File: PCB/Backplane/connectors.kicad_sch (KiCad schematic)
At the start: 10 parts, among them J2 Front, J3 Rear, J4 Bus In, J5 Bus Out, J6 Power In, J7 Power Out, U10 CM1293A‐04SO, U9 CM1293A‐04SO

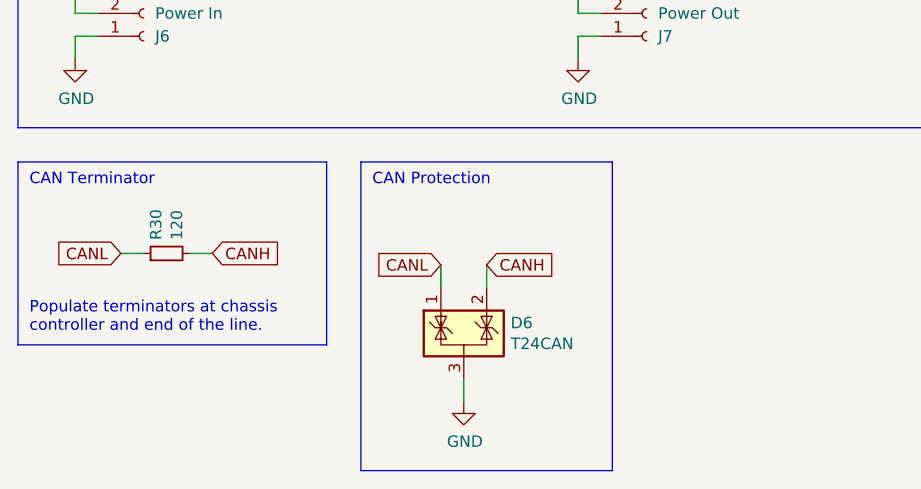
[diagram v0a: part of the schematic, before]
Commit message: Add ESD protection to the RS485 networks.
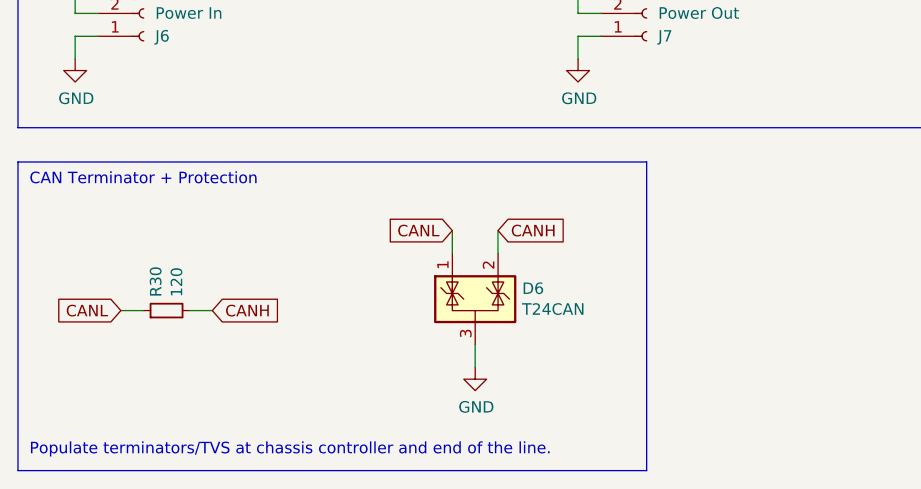
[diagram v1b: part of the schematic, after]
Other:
- note added: "CAN Terminator + Protection"
- note added: "Populate terminators/TVS at chassis controller and end of the line."
- note removed: "CAN Protection"
- note removed: "CAN Terminator"
- note removed: "Populate terminators at chassis controller and end of the line."
- moved on the sheet: D6, R30
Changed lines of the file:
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@@
 	(rectangle
 		(start 15.24 132.08)
-		(end 49.53 152.4)
+		(end 85.09 166.37)
 		(stroke
 			(width 0)
@@
 	)
 	(rectangle
-		(start 53.34 132.08)
-		(end 81.28 166.37)
-		(stroke
-			(width 0)
-			(type default)
-		)
-		(fill
-			(type none)
-		)
-	)
-	(rectangle
 		(start 165.1 15.24)
 		(end 275.59 71.12)
@@
 		)
 	)
-	(text "CAN Terminator"
+	(text "CAN Terminator + Protection"
 		(exclude_from_sim no)
 		(at 16.51 133.35 0)
@@
 		)
 	)
-	(text "Populate terminators at chassis\ncontroller and end of the line."
+	(text "Populate terminators/TVS at chassis controller and end of the line."
 		(exclude_from_sim no)
-		(at 16.51 151.13 0)
+		(at 16.51 164.846 0)
 		(effects
 			(font
@@
 		(exclude_from_sim no)
 		(at 166.37 16.51 0)
-		(effects
-			(font
-				(size 1.27 1.27)
-			)
-			(justify left top)
-		)
-	)
-	(text "CAN Protection"
-		(exclude_from_sim no)
-		(at 54.61 133.35 0)
 		(effects
 			(font
@@
 	(wire
 		(pts
-			(xy 64.77 156.21) (xy 64.77 158.75)
+			(xy 66.04 152.4) (xy 66.04 154.94)
 		)
 		(stroke
@@
 	(wire
 		(pts
-			(xy 26.67 142.24) (xy 29.21 142.24)
+			(xy 26.67 148.59) (xy 29.21 148.59)
 		)
 		(stroke
@@
 	(wire
 		(pts
-			(xy 67.31 143.51) (xy 67.31 146.05)
+			(xy 68.58 139.7) (xy 68.58 142.24)
 		)
 		(stroke
@@
 	(wire
 		(pts
-			(xy 62.23 143.51) (xy 62.23 146.05)
+			(xy 63.5 139.7) (xy 63.5 142.24)
 		)
 		(stroke
@@
 	(wire
 		(pts
-			(xy 36.83 142.24) (xy 34.29 142.24)
+			(xy 36.83 148.59) (xy 34.29 148.59)
 		)
 		(stroke
@@
 	(global_label "CANH"
 		(shape input)
-		(at 36.83 142.24 0)
+		(at 36.83 148.59 0)
 		(fields_autoplaced yes)
 		(effects
@@
 		)
 		(property "Intersheetrefs" "${INTERSHEET_REFS}"
-			(at 44.8348 142.24 0)
+			(at 44.8348 148.59 0)
 			(effects
 				(font
@@
 	(global_label "CANL"
 		(shape input)
-		(at 26.67 142.24 180)
+		(at 26.67 148.59 180)
 		(fields_autoplaced yes)
 		(effects
@@
 		)
 		(property "Intersheetrefs" "${INTERSHEET_REFS}"
-			(at 19.6218 142.24 0)
+			(at 19.6218 148.59 0)
 			(effects
 				(font
@@
 	(global_label "CANL"
 		(shape input)
-		(at 62.23 143.51 180)
+		(at 63.5 139.7 180)
 		(fields_autoplaced yes)
 		(effects
@@
 		)
 		(property "Intersheetrefs" "${INTERSHEET_REFS}"
-			(at 55.1818 143.51 0)
+			(at 56.4518 139.7 0)
 			(effects
 				(font
@@
 	(global_label "CANH"
 		(shape input)
-		(at 67.31 143.51 0)
+		(at 68.58 139.7 0)
 		(fields_autoplaced yes)
 		(effects
@@
 		)
 		(property "Intersheetrefs" "${INTERSHEET_REFS}"
-			(at 74.6606 143.51 0)
+			(at 75.9306 139.7 0)
 			(effects
 				(font
@@
 	(symbol
 		(lib_id "Power_Protection:NUP2105L")
-		(at 64.77 151.13 0)
+		(at 66.04 147.32 0)
 		(unit 1)
 		(exclude_from_sim no)
@@
 		(dnp no)
 		(property "Reference" "D6"
-			(at 69.977 149.9616 0)
+			(at 71.247 146.1516 0)
 			(effects
 				(font
@@
 		)
 		(property "Value" "T24CAN"
-			(at 69.977 152.273 0)
+			(at 71.247 148.463 0)
 			(effects
 				(font
@@
 		)
 		(property "Footprint" "Package_TO_SOT_SMD:SOT-23"
-			(at 70.485 152.4 0)
+			(at 71.755 148.59 0)
 			(effects
 				(font
@@
 		)
 		(property "Datasheet" "https://www.onsemi.com/pub_link/Collateral/NUP2105L-D.PDF"
-			(at 67.945 147.955 0)
+			(at 69.215 144.145 0)
 			(effects
 				(font
@@
 		)
 		(property "Description" "Dual Line CAN Bus Protector, 24Vrwm"
-			(at 64.77 151.13 0)
+			(at 66.04 147.32 0)
 			(effects
 				(font
@@
 		)
 		(property "DIGIKEY" "STOCK"
-			(at 64.77 151.13 0)
+			(at 66.04 147.32 0)
 			(effects
 				(font
@@
 		)
 		(property "Sim.Device" ""
-			(at 64.77 151.13 0)
+			(at 66.04 147.32 0)
 			(effects
 				(font
@@
 		)
 		(property "Sim.Pins" ""
-			(at 64.77 151.13 0)
+			(at 66.04 147.32 0)
 			(effects
 				(font
@@
 	(symbol
 		(lib_id "power:GND")
-		(at 64.77 158.75 0)
+		(at 66.04 154.94 0)
 		(unit 1)
 		(exclude_from_sim no)
@@
 		(dnp no)
 		(property "Reference" "#PWR086"
-			(at 64.77 165.1 0)
+			(at 66.04 161.29 0)
 			(effects
 				(font
@@
 		)
 		(property "Value" "GND"
-			(at 64.897 163.1442 0)
+			(at 66.167 159.3342 0)
 			(effects
 				(font
@@
 		)
 		(property "Footprint" ""
-			(at 64.77 158.75 0)
+			(at 66.04 154.94 0)
 			(effects
 				(font
@@
 		)
 		(property "Datasheet" ""
-			(at 64.77 158.75 0)
+			(at 66.04 154.94 0)
 			(effects
 				(font
@@
 		)
 		(property "Description" "Power symbol creates a global label with name \"GND\" , ground"
-			(at 64.77 158.75 0)
+			(at 66.04 154.94 0)
 			(effects
 				(font
@@
 	(symbol
 		(lib_id "Device:R_Small")
-		(at 31.75 142.24 90)
+		(at 31.75 148.59 90)
 		(unit 1)
 		(exclude_from_sim no)
@@
 		(dnp no)
 		(property "Reference" "R30"
-			(at 30.5816 140.7414 0)
+			(at 30.5816 147.0914 0)
 			(effects
 				(font
@@
 		)
 		(property "Value" "120"
-			(at 32.893 140.7414 0)
+			(at 32.893 147.0914 0)
 			(effects
 				(font
@@
 		)
 		(property "Footprint" "Resistor_SMD:R_0603_1608Metric"
-			(at 31.75 142.24 0)
+			(at 31.75 148.59 0)
 			(effects
 				(font
@@
 		)
 		(property "Datasheet" "~"
-			(at 31.75 142.24 0)
+			(at 31.75 148.59 0)
 			(effects
 				(font
@@
 		)
 		(property "Description" ""
-			(at 31.75 142.24 0)
+			(at 31.75 148.59 0)
 			(effects
 				(font
@@
 		)
 		(property "DIGIKEY" "P120HCT-ND"
-			(at 31.75 142.24 0)
-			(effects
-				(font
+			(at 31.75 148.59 0)
+			(effects
+				(font

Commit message: Correct Digikey part numbers.
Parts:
- D6: DIGIKEY STOCK -> CDSOT23-T24CANCT-ND
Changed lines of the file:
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@@
 			)
 		)
-		(property "DIGIKEY" "STOCK"
+		(property "DIGIKEY" "CDSOT23-T24CANCT-ND"
 			(at 66.04 147.32 0)
 			(effects
